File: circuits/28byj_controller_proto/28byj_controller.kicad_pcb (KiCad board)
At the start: 2 copper layers, 50 x 50 mm, 17 parts, among them J1 INPUT, J2 5V, M1 28BYJ-48_Stepper, M2 28BYJ-48_Stepper, U1 74HC595, U2 ULN2803A

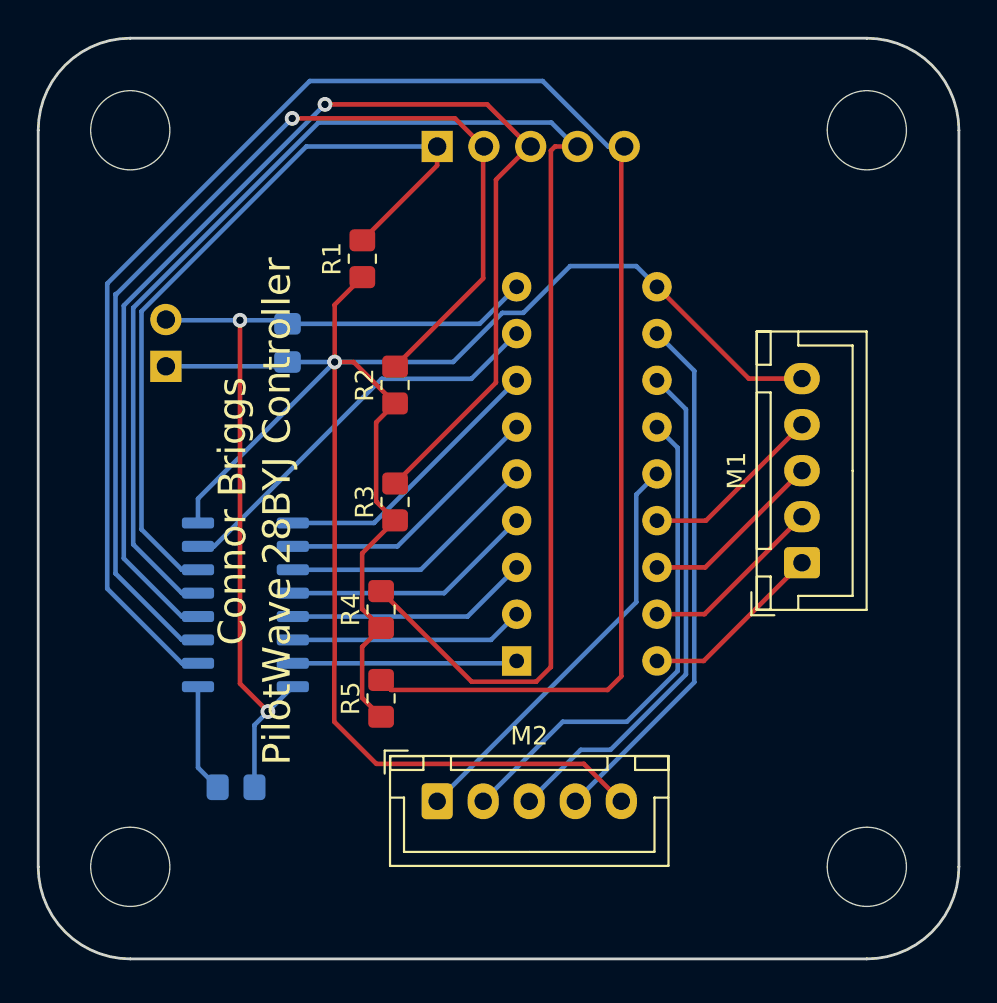
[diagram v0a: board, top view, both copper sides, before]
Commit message: Code works and is tested on waveforms.
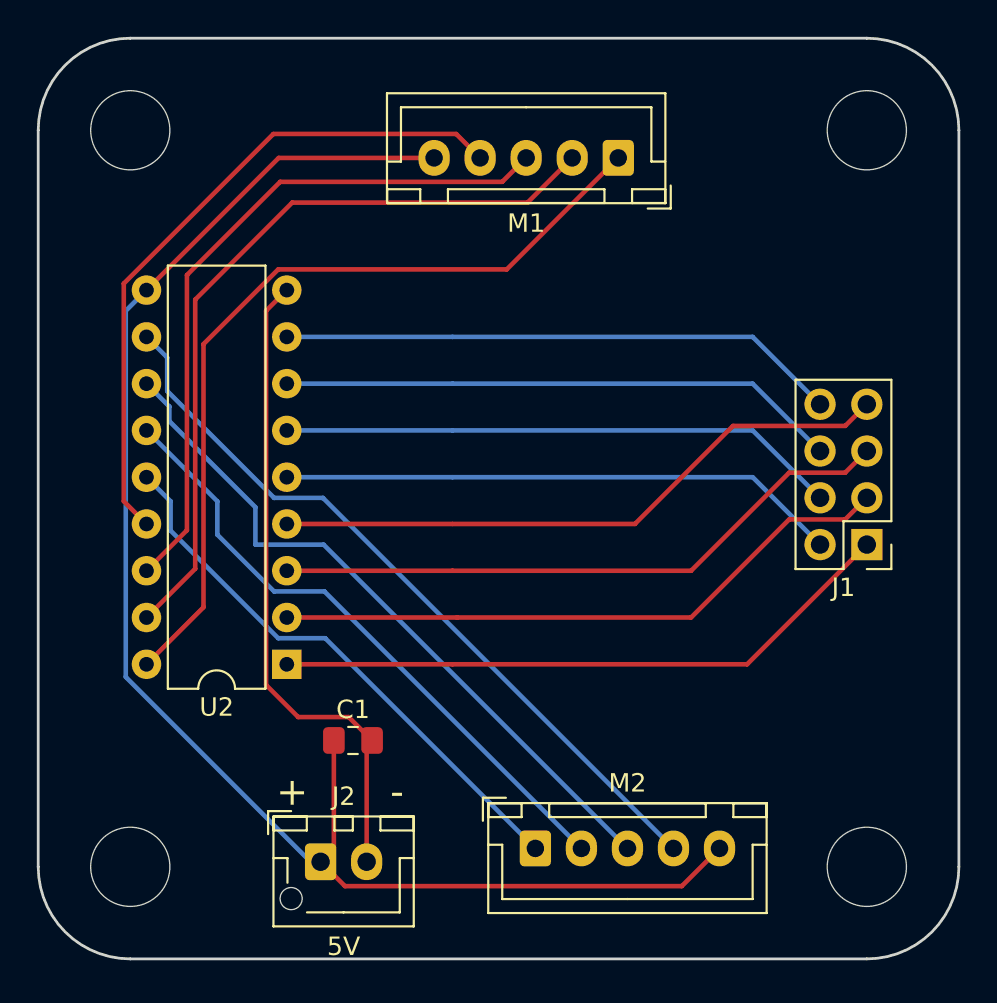
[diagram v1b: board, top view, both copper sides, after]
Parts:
- removed R1, R2, R3, R4, R5: 10K, Resistor_SMD:R_0805_2012Metric_Pad1.20x1.40mm_HandSolder
- removed R6: 1K, Resistor_SMD:R_0805_2012Metric_Pad1.20x1.40mm_HandSolder
- removed U1: 74HC595, Package_SO:SO-16_3.9x9.9mm_P1.27mm
- C1, U2: moved to F.Cu
- J1: value INPUT -> Input; footprint Connector_PinSocket_2.54mm:PinSocket_1x05_P2.54mm_Vertical -> Connector_PinHeader_2.54mm:PinHeader_2x04_P2.54mm_Vertical; moved to F.Cu
- J2: footprint Connector_PinSocket_2.54mm:PinSocket_1x02_P2.54mm_Vertical -> Connector_JST:JST_XH_B2B-XH-AM_1x02_P2.50mm_Vertical; moved to F.Cu
- moved J1 31.8 mm to (145.0, 77.5), turned to 180 degrees
- moved J2 28.2 mm to (115.3, 94.7)
- moved M1 24.1 mm to (131.5, 56.5), turned to 180 degrees
- moved C1 21.9 mm to (117.1, 88.1), turned to 0 degrees
- moved U2 12.5 mm to (113.5, 84.0), turned to 180 degrees
- moved M2 5.92 mm to (127.0, 94.0)
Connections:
- U2 pad 1: Net-(U1-Pad7) -> Net-(J1-Pad1)
- U2 pad 2: Net-(U1-Pad6) -> Net-(J1-Pad2)
- U2 pad 3: Net-(U1-Pad5) -> Net-(J1-Pad3)
- U2 pad 4: Net-(U1-Pad4) -> Net-(J1-Pad4)
- U2 pad 5: Net-(U1-Pad3) -> Net-(J1-Pad5)
- U2 pad 6: Net-(U1-Pad2) -> Net-(J1-Pad6)
- U2 pad 7: Net-(U1-Pad1) -> Net-(J1-Pad7)
- U2 pad 8: Net-(U1-Pad15) -> Net-(J1-Pad8)
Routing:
- net Net-(J1-Pad5): track 99.5 -> 30.5 mm
- net Net-(J1-Pad4): track 87.2 -> 34.2 mm
- net Net-(M1-Pad1): track 10.1 -> 45.4 mm
- net Net-(J1-Pad3): track 67.9 -> 34.2 mm, vias 1 -> 0
- net +5V: track 117.4 -> 84.8 mm, vias 1 -> 0
- net Net-(M1-Pad2): track 10.1 -> 42.0 mm
- net Net-(J1-Pad8): track 0.00 -> 30.5 mm
- net Net-(J1-Pad7): track 0.00 -> 30.5 mm
- net Net-(J1-Pad6): track 0.00 -> 30.5 mm
- net Net-(M1-Pad3): track 10.1 -> 38.0 mm
- net Net-(M1-Pad4): track 10.0 -> 36.8 mm
- net Net-(J1-Pad2): track 59.6 -> 34.2 mm, vias 1 -> 0
- net Net-(U1-Pad15): track 22.1 -> 0.00 mm
- net Net-(U1-Pad1): track 15.4 -> 0.00 mm
- net Net-(U1-Pad2): track 14.8 -> 0.00 mm
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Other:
- board text removed: "1"
- board text removed: "Connor Briggs PilotWave 28BYJ Controller"

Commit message: Modified some circuits.
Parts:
- added R1: 10 K, Resistor_SMD:R_0805_2012Metric_Pad1.20x1.40mm_HandSolder, F.Cu at (136.9, 82.8)
- added R2: 10 K, Resistor_SMD:R_0805_2012Metric_Pad1.20x1.40mm_HandSolder, F.Cu at (136.9, 66.8)
- added R3: 10 K, Resistor_SMD:R_0805_2012Metric_Pad1.20x1.40mm_HandSolder, B.Cu at (136.9, 72.1)
- added R4: 10 K, Resistor_SMD:R_0805_2012Metric_Pad1.20x1.40mm_HandSolder, B.Cu at (136.9, 66.8)
- added R5: 10 K, Resistor_SMD:R_0805_2012Metric_Pad1.20x1.40mm_HandSolder, F.Cu at (136.9, 77.5)
- added R6: 10 K, Resistor_SMD:R_0805_2012Metric_Pad1.20x1.40mm_HandSolder, B.Cu at (136.9, 77.5)
- added R7: 10 K, Resistor_SMD:R_0805_2012Metric_Pad1.20x1.40mm_HandSolder, F.Cu at (136.9, 72.1)
- added R8: 10 K, Resistor_SMD:R_0805_2012Metric_Pad1.20x1.40mm_HandSolder, B.Cu at (136.9, 82.8)
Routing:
- net +5V: track 84.8 -> 205.7 mm, vias 0 -> 6
- net Net-(J1-Pad5): track 30.5 -> 36.1 mm
- net Net-(J1-Pad6): track 30.5 -> 33.4 mm
- net Net-(J1-Pad4): track 34.2 -> 35.9 mm
- net Net-(J1-Pad3): track 34.2 -> 35.2 mm
